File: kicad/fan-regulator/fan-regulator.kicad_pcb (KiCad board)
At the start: 2 copper layers, 50.8 x 53.3 mm, 13 parts, among them IC1 TR-72D, J1 Barrel_Jack, J2 Conn_01x04_Male, U1 LM7805_TO220, U2 MCP1700-3002E_SOT23

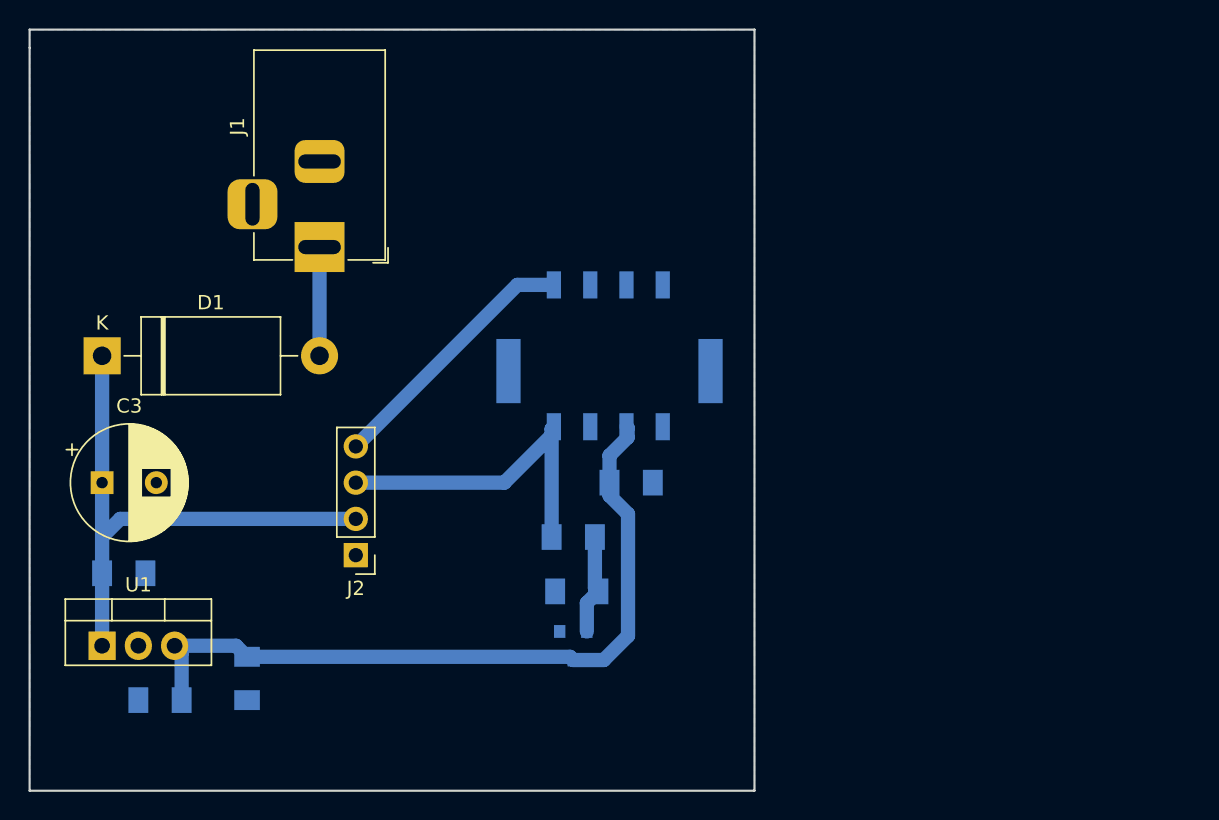
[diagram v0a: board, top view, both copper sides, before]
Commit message: Fix bugs in KiCAD EDA's files
Signed-off-by: Roman Ondráček <ondracek.roman@centrum.cz>
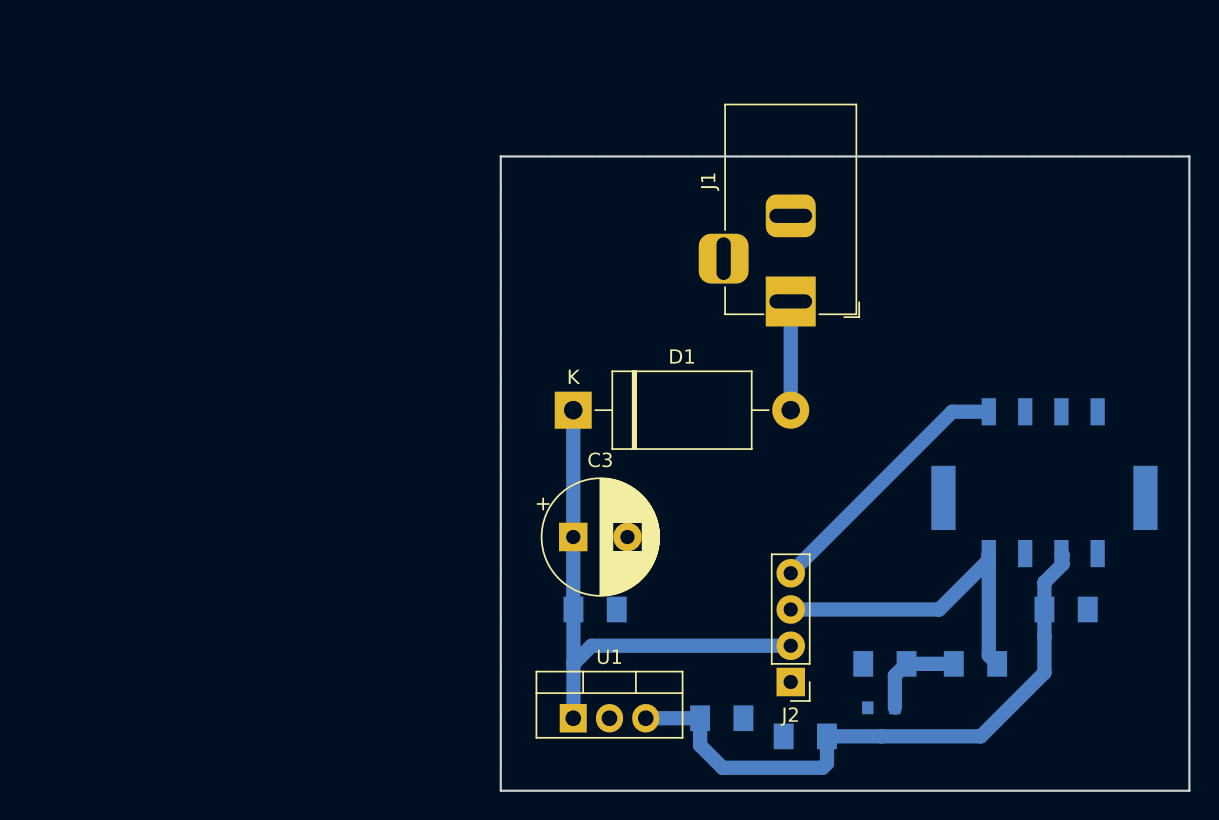
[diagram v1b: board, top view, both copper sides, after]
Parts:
- moved C4 39.4 mm to (137.4, 110.5), turned to 0 degrees
- moved C2 39.3 mm to (143.3, 111.8), turned to 180 degrees
- moved U1 33.4 mm to (127.0, 110.5)
- moved J1 33.2 mm to (142.2, 81.3)
- moved C3 33.2 mm to (127.0, 97.8)
- moved D1 33.2 mm to (127.0, 88.9)
- moved C1 33.1 mm to (128.5, 102.9)
- moved IC1 31.8 mm to (160.0, 94.0)
- moved J2 31.8 mm to (142.2, 108.0)
- moved C6 31.7 mm to (161.5, 102.9)
- moved R1 29.6 mm to (155.2, 106.7), turned to 0 degrees
- moved U2 22.2 mm to (148.6, 110.8)
- moved C5 22.2 mm to (148.8, 106.7)
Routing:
- net +5V: track 52.7 -> 43.3 mm
- net +12V: track 38.6 -> 37.4 mm
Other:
- board size 50.8 x 53.3 mm -> 48.3 x 44.4 mm
